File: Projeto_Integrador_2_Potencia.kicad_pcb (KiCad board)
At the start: 2 copper layers, 35 x 31.5 mm, 4 parts, among them J1 Conn_01x03_Pin, Q1 IRF740, U1 INA219AxD

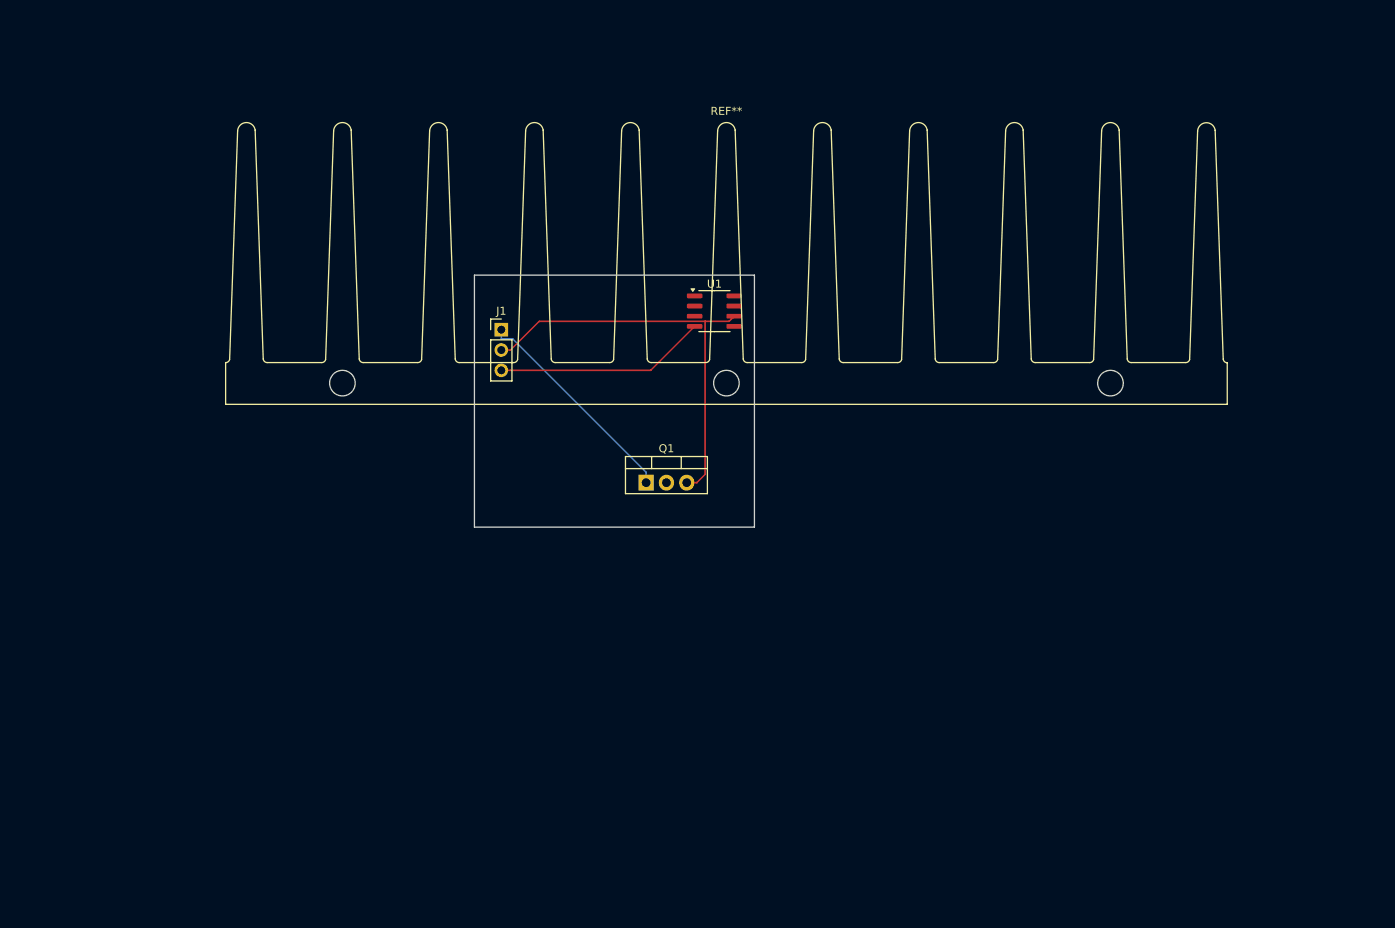
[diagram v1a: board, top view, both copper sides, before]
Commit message: Esquemático Finalizado + Começo Layout
-Precisa confirmar tamanho do Indutor
-Precisa Trocar mosfet de lugar(devido ao dissipador)
-Ao definir locais de componentes, fazer trilhas
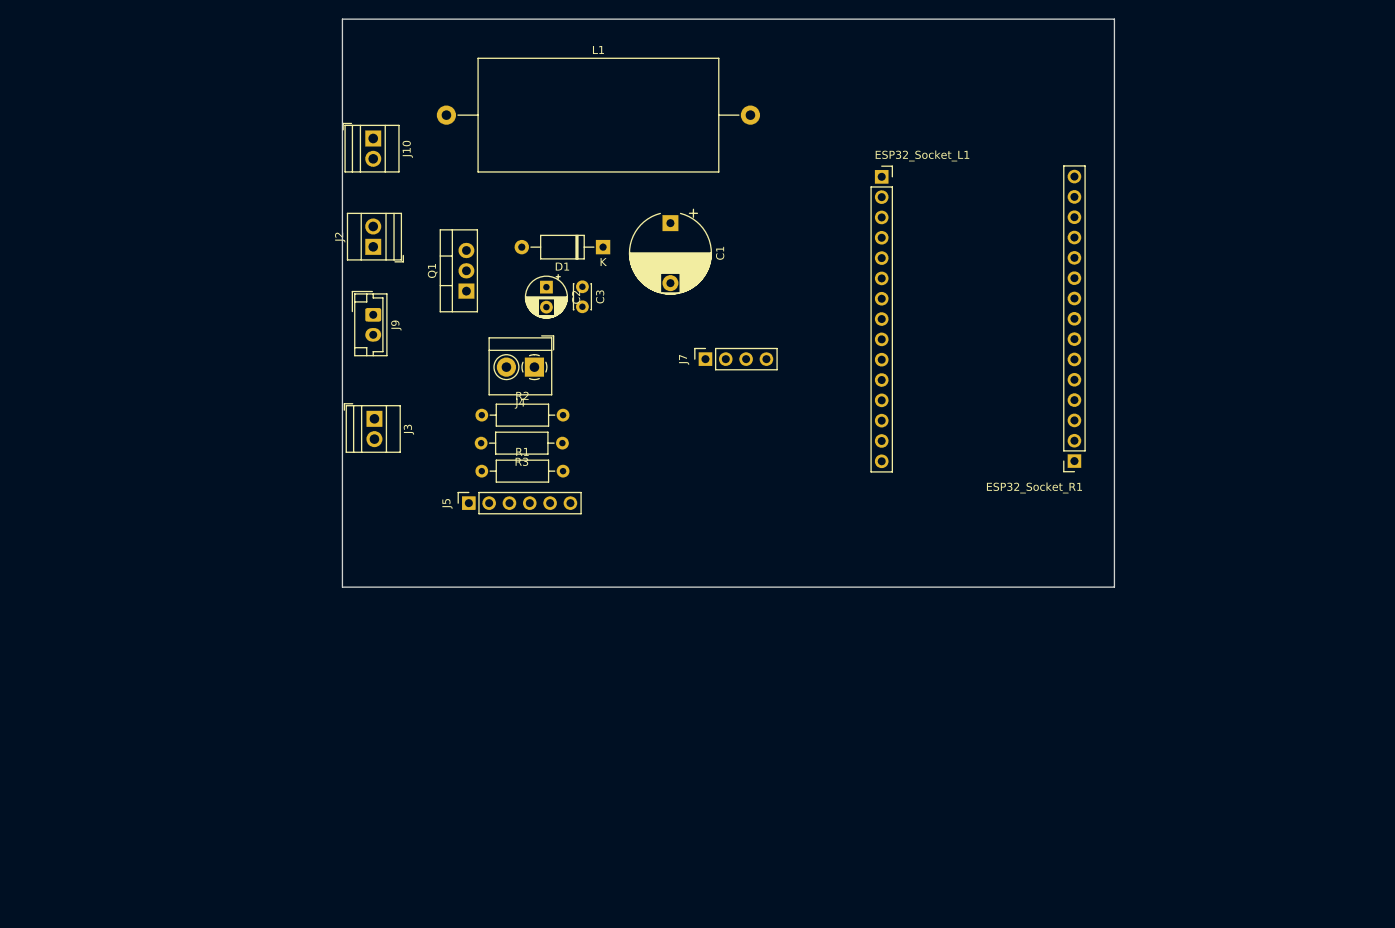
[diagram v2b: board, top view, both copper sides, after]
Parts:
- removed J1: Conn_01x03_Pin, Connector_PinHeader_2.54mm:PinHeader_1x03_P2.54mm_Vertical
- removed REF**: Heatsink_125x35x50mm_3xFixationM3, Heatsink:Heatsink_125x35x50mm_3xFixationM3
- removed U1: INA219AxD, Package_SO:SOIC-8_3.9x4.9mm_P1.27mm
- added C1: 100uF, Capacitor_THT:CP_Radial_D10.0mm_P7.50mm, F.Cu at (126.0, 64.5)
- added C2: 22uF, Capacitor_THT:CP_Radial_D5.0mm_P2.50mm, F.Cu at (110.5, 72.5)
- added C3: 2.2uF, Capacitor_THT:C_Disc_D3.0mm_W2.0mm_P2.50mm, F.Cu at (115.0, 72.5)
- added D1: ~, Diode_THT:D_A-405_P10.16mm_Horizontal, F.Cu at (117.6, 67.5)
- added ESP32_Socket_L1: ~, Connector_PinSocket_2.54mm:PinSocket_1x15_P2.54mm_Vertical, F.Cu at (152.4, 58.7)
- added ESP32_Socket_R1: ~, Connector_PinSocket_2.54mm:PinSocket_1x15_P2.54mm_Vertical, F.Cu at (176.5, 94.2)
- added J10: Borne_CMD_Interface, TerminalBlock:TerminalBlock_Xinya_XY308-2.54-2P_1x02_P2.54mm_Horizontal, F.Cu at (88.8, 53.9)
- added J2: Vi 24V, TerminalBlock:TerminalBlock_Xinya_XY308-2.54-2P_1x02_P2.54mm_Horizontal, F.Cu at (88.8, 67.5)
- added J3: Vo 48V, TerminalBlock:TerminalBlock_Xinya_XY308-2.54-2P_1x02_P2.54mm_Horizontal, F.Cu at (89.0, 89.0)
- added J4: INA219_01x02_Socket_3.5mm, TerminalBlock_4Ucon:TerminalBlock_4Ucon_1x02_P3.50mm_Horizontal, F.Cu at (109.0, 82.5)
- added J5: INA219_01x06_Socket_2.55mm, Connector_PinSocket_2.54mm:PinSocket_1x06_P2.54mm_Vertical, F.Cu at (100.8, 99.5)
- added J7: Display_01x04_Socket, Connector_PinSocket_2.54mm:PinSocket_1x04_P2.54mm_Vertical, F.Cu at (130.4, 81.5)
- added J9: JST_01x02_Pin, Connector_JST:JST_EH_B2B-EH-A_1x02_P2.50mm_Vertical, F.Cu at (88.8, 76.0)
- added L1: 1.44mH, Inductor_THT:L_Axial_L29.9mm_D14.0mm_P38.00mm_Horizontal_Vishay_IHA-105, F.Cu at (98.0, 51.0)
- added R1: 10k, Resistor_THT:R_Axial_DIN0207_L6.3mm_D2.5mm_P10.16mm_Horizontal, F.Cu at (102.4, 95.5)
- added R2: 82k, Resistor_THT:R_Axial_DIN0207_L6.3mm_D2.5mm_P10.16mm_Horizontal, F.Cu at (102.4, 88.5)
- added R3: 300, Resistor_THT:R_Axial_DIN0207_L6.3mm_D2.5mm_P10.16mm_Horizontal, F.Cu at (112.5, 92.0)
- moved Q1 32.8 mm to (100.5, 73.0), turned to 90 degrees
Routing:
- net GND: track 52.7 -> 0.00 mm
- net pwm: track 27.5 -> 0.00 mm
- net fb1: track 26.4 -> 0.00 mm
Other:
- board size 35 x 31.5 mm -> 96.5 x 71 mm
- board text added: "Display OLED 0.96″"
- board text added: "ESP32 DevKitV1 30P"
- board text added: "INA219"
- board text added: "Indutor"

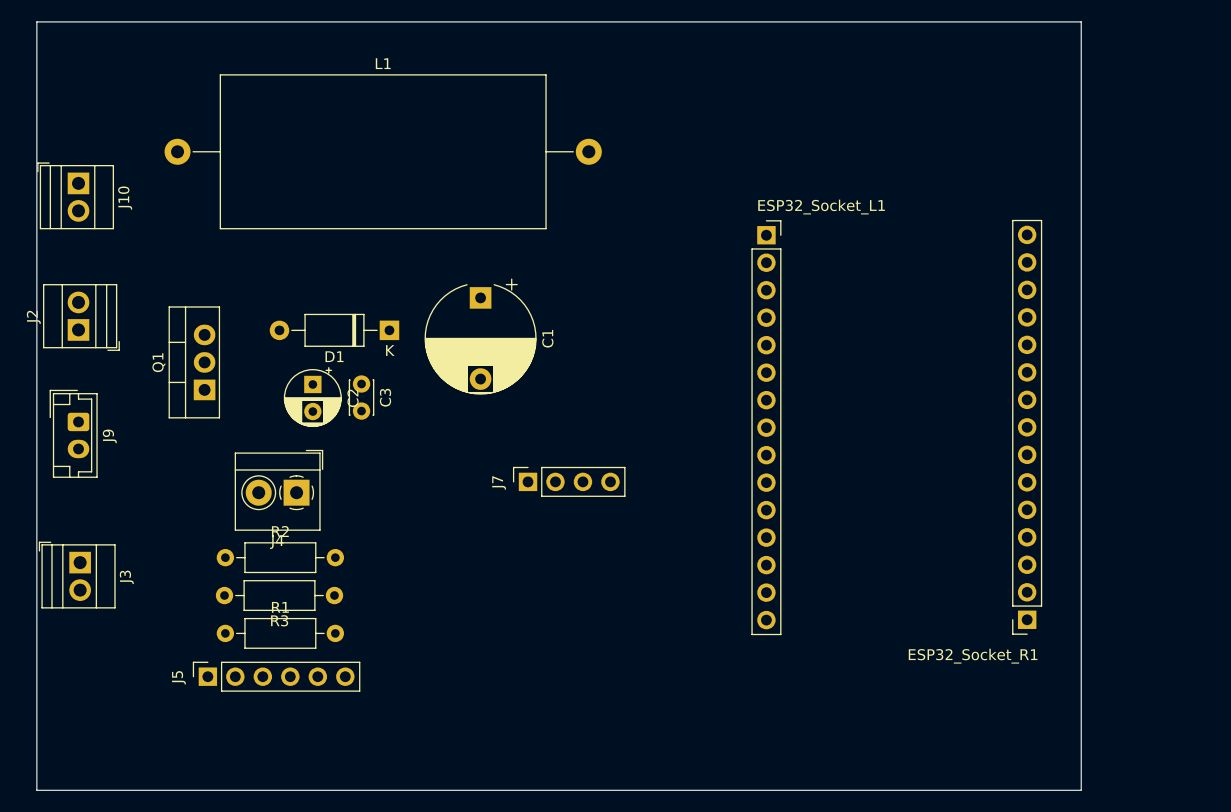
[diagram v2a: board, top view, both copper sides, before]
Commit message: Aplicação de recomendações Texas Instruments para layout e disposição de trilhas
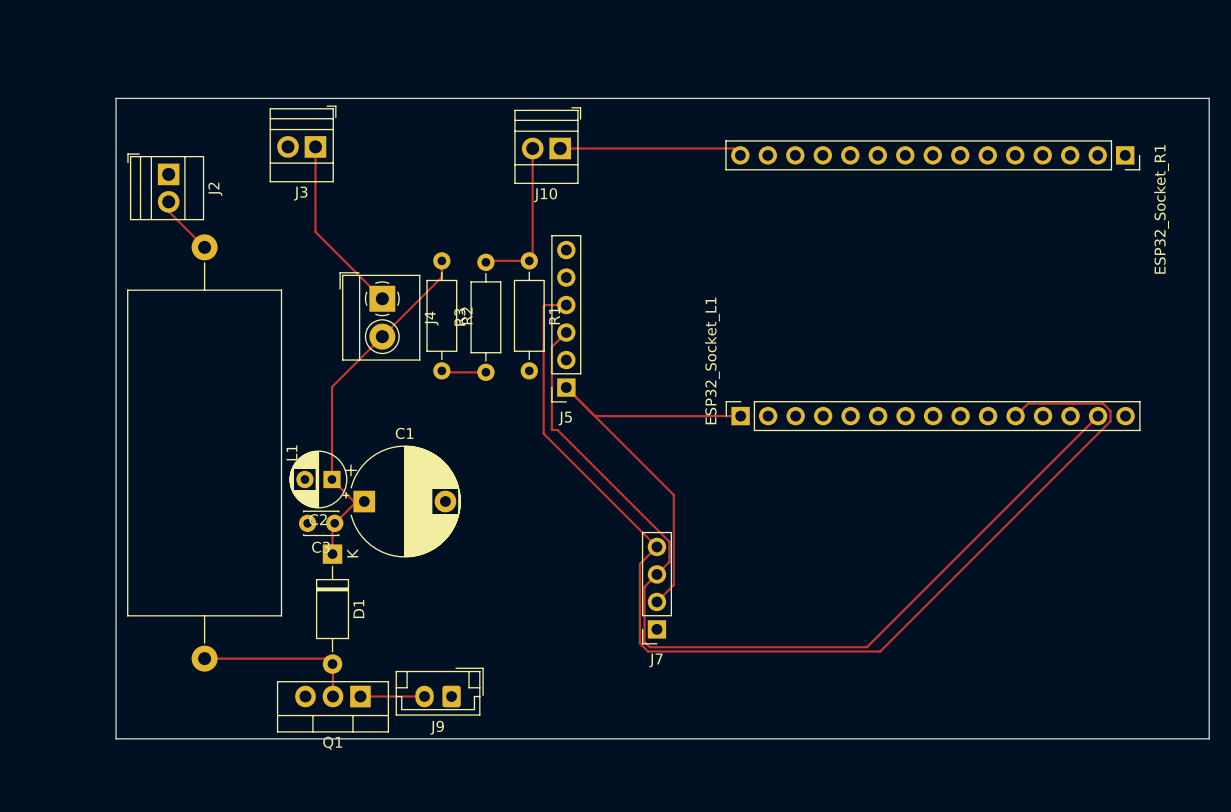
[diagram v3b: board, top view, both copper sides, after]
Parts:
- moved J10 44.6 mm to (133.4, 50.7), turned to 180 degrees
- moved R1 44.4 mm to (130.5, 61.1), turned to -90 degrees
- moved J3 44.1 mm to (110.7, 50.5), turned to 180 degrees
- moved ESP32_Socket_R1 43.9 mm to (185.6, 51.3), turned to -90 degrees
- moved J9 42.8 mm to (123.3, 101.3), turned to 180 degrees
- moved J5 42.6 mm to (133.9, 72.8), turned to 180 degrees
- moved R2 33.9 mm to (122.4, 61.1), turned to -90 degrees
- moved Q1 31.8 mm to (114.9, 101.3), turned to 180 degrees
- moved R3 24.9 mm to (126.5, 71.4), turned to 90 degrees
- moved C1 21.7 mm to (115.3, 83.3), turned to 0 degrees
- moved D1 21.3 mm to (112.3, 88.2), turned to -90 degrees
- moved J4 19.6 mm to (116.9, 64.6), turned to -90 degrees
- moved J7 18.1 mm to (142.3, 95.1), turned to 180 degrees
- moved ESP32_Socket_L1 16.9 mm to (150.0, 75.4), turned to 90 degrees
- moved J2 16.6 mm to (97.2, 53.1), turned to -90 degrees
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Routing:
- net I2C_Sda: track 0.00 -> 101.4 mm
- net I2C_Scl: track 0.00 -> 85.8 mm
- net 3V3: track 0.00 -> 41.8 mm
- net INA_Vin-: track 0.00 -> 34.7 mm
- net 12V: track 0.00 -> 16.9 mm
- net INA_Vin+: track 0.00 -> 16.6 mm
- net Net-(D1-A): track 0.00 -> 15.8 mm
- net 5.2V_feedback: track 0.00 -> 14.6 mm
- net pwm: track 0.00 -> 5.92 mm
- net Net-(J2-Pin_2): track 0.00 -> 5.58 mm
- net Net-(R2-Pad2): track 0.00 -> 4.13 mm
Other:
- board size 96.5 x 71 mm -> 101 x 59.2 mm
- board text removed: "Indutor"

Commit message: Adição de footprint e símbolo do ESP32
Atualização das trilhas da PCB
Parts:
- removed ESP32_Socket_L1, ESP32_Socket_R1: ~, Connector_PinSocket_2.54mm:PinSocket_1x15_P2.54mm_Vertical
- added U1: ESP32-DEVKIT-V1, footprints_and_symbols:MODULE_ESP32_DEVKIT_V1, F.Cu at (165.4, 88.6)
- J9: value JST_01x02_Pin -> PWM_Connector
- moved J7 33.1 mm to (153.6, 64.0)
- moved J9 6.56 mm to (129.9, 101.6)
- moved D1 6.56 mm to (118.9, 88.4)
- moved Q1 6.56 mm to (121.5, 101.6)
- moved J2 5.71 mm to (91.9, 50.8), turned to 180 degrees
- moved C1 5.63 mm to (120.9, 83.3)
- moved C2 5.13 mm to (117.4, 81.0)
- moved C3 4.85 mm to (117.4, 85.6)
- moved L1 2.79 mm to (97.7, 59.8)
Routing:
- net 12V: track 16.9 -> 104.7 mm
- net 3V3: track 41.8 -> 81.5 mm
- net I2C_Sda: track 101.4 -> 66.6 mm
- net I2C_Scl: track 85.8 -> 53.9 mm
- net INA_Vin-: track 34.7 -> 22.6 mm
- net Net-(D1-A): track 15.8 -> 26.0 mm
- net Net-(J2-Pin_2): track 5.58 -> 12.5 mm
- added copper zone on F.Cu, net GND
- added copper zone on F.Cu, net INA_Vin-
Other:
- board size 101 x 59.2 mm -> 110.7 x 59.4 mm
- board text removed: "ESP32 DevKitV1 30P"

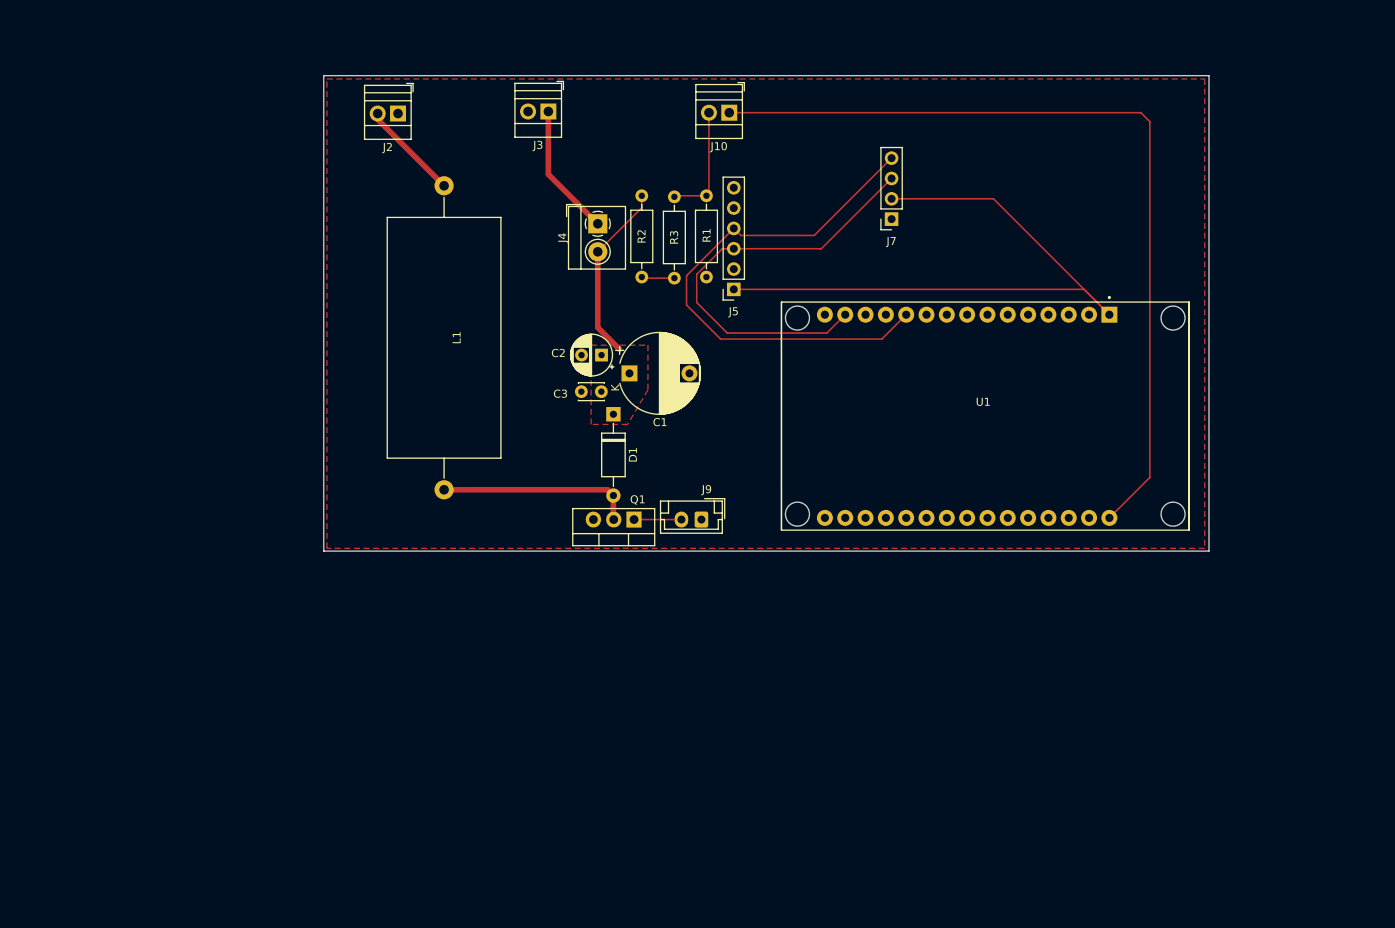
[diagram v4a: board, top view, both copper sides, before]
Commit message: Correções do layout da pcb e alinhamento do grupo
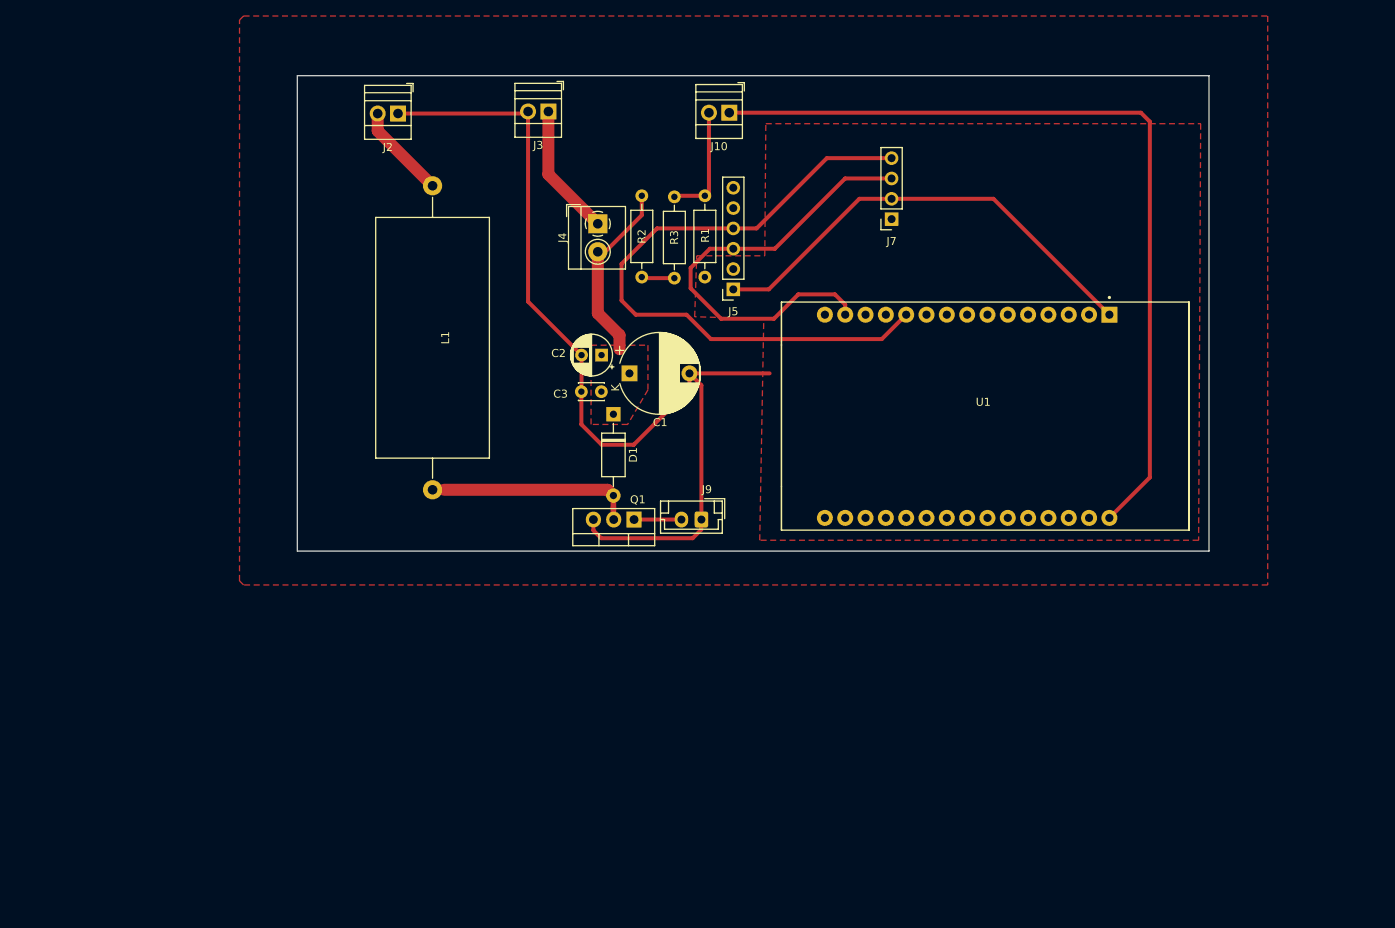
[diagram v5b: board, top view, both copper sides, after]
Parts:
- moved L1 1.44 mm to (96.3, 59.8)
- moved R1 0.20 mm to (130.3, 61.1)
- moved J5 0.06 mm to (133.9, 72.8)
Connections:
- net 12V renamed 8V
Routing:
- net GND: track 0.00 -> 123.5 mm
- net 3V3: track 81.5 -> 57.6 mm
- net I2C_Sda: track 66.6 -> 82.6 mm
- net I2C_Scl: track 53.9 -> 56.2 mm
- net Net-(J2-Pin_2): track 12.5 -> 11.9 mm
- net INA_Vin-: track 22.6 -> 23.1 mm
- added copper zone on F.Cu, net (none)
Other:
- board size 110.7 x 59.4 mm -> 114 x 59.4 mm
